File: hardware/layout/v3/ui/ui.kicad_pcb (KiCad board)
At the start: 4 copper layers, 13.8 x 40.5 mm, 25 parts, among them J1 Carrier, J2 OLED ZIF, SW1 PRG/RST, SW2 FUNC, U1 74AHCT1G125

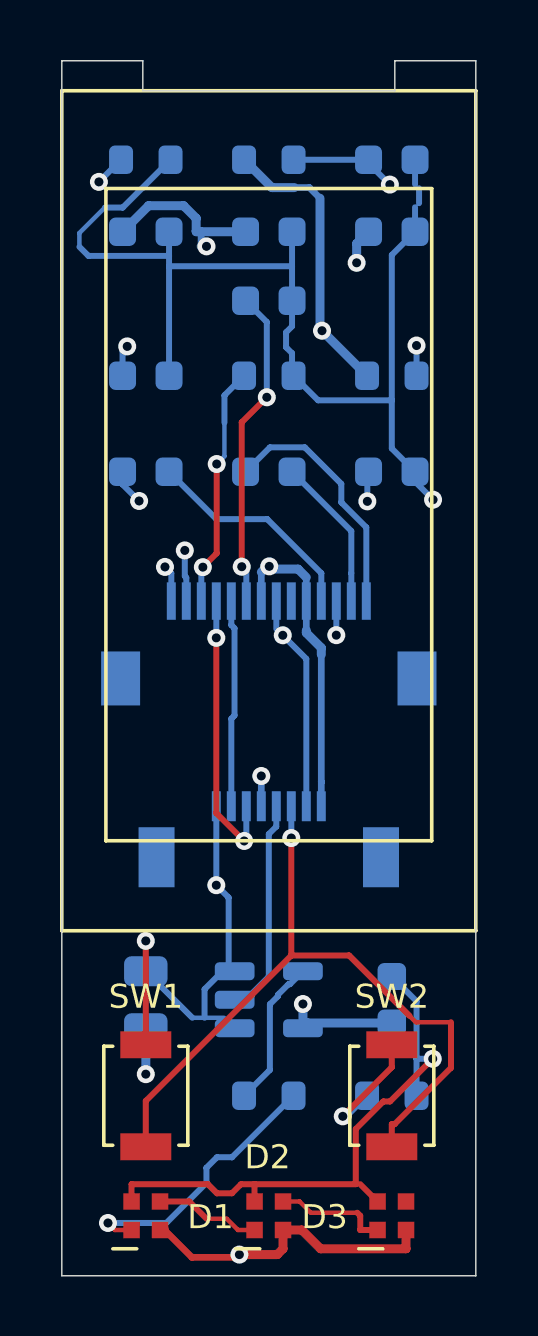
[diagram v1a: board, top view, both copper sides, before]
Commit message: Replaced V3 OLED connector from 14-pin 0.5mm ZIF FPC to 14-pin 0.62mm pitch direct-solder FPC footprint, relocated UI board passives to accommodate new layout with top-edge notch adjusted to 9.8mm width for 12mm flex tail, and updated assembly documentation with NFP1312-15AY part number and pre-applied mounting tape details
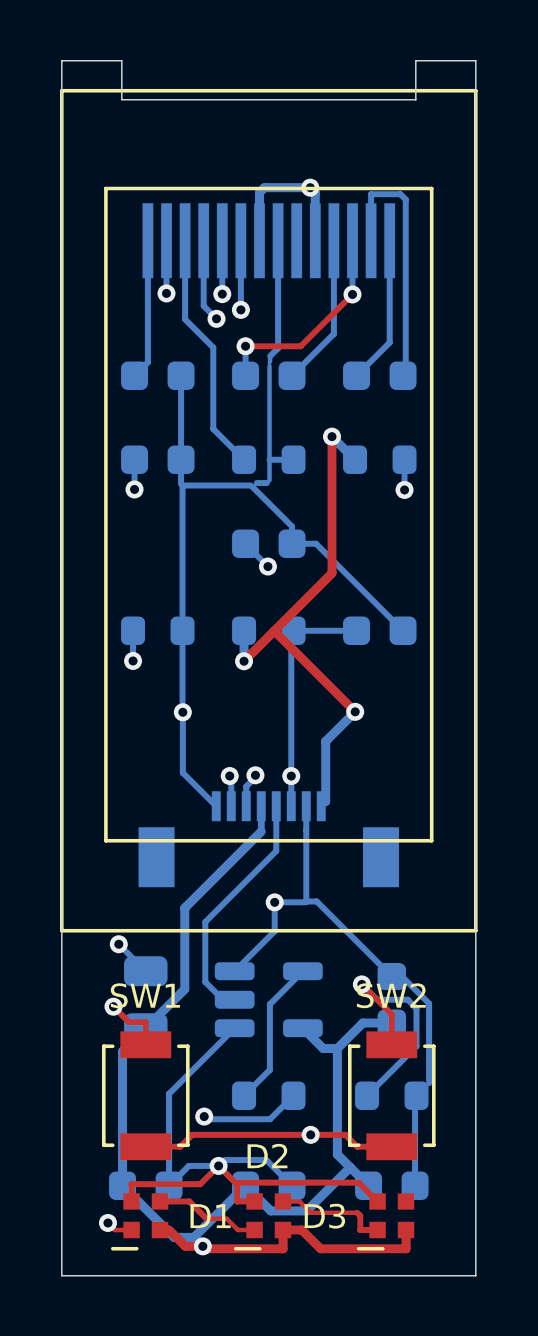
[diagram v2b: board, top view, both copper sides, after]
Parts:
- J2: value OLED ZIF -> OLED; footprint gateway_fp:FPC_XUNPU_FPC-05F-14PH20 -> gateway_fp:OLED_FPC_14P_P0.62mm_Hotbar
- moved C4 31.8 mm to (2.80, -3.00)
- moved C5 31.8 mm to (6.90, -3.00)
- moved C6 31.8 mm to (11.0, -3.00)
- moved C1 15.7 mm to (10.6, -21.5)
- moved R2 15.7 mm to (3.20, -21.5)
- moved R1 15.7 mm to (6.90, -21.5)
- moved J2 13.3 mm to (6.90, -34.5)
- moved C7 8.10 mm to (6.90, -24.4)
- moved C10 7.81 mm to (3.20, -27.2)
- moved C8 5.20 mm to (6.90, -30.0)
- moved C9 4.89 mm to (10.6, -30.0)
- moved R5 2.83 mm to (10.6, -27.2)
- moved R6 2.80 mm to (6.90, -27.2)
- moved C11 0.40 mm to (3.20, -30.0)
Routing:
- net +5V: track 72.7 -> 43.5 mm, vias 6 -> 1
- net BTN_LADDER: track 53.3 -> 28.7 mm
- net I2C_SCL: track 6.93 -> 24.1 mm, vias 0 -> 2
- net N$1: track 31.0 -> 15.2 mm
- net I2C_SDA: track 9.57 -> 19.9 mm
- net OLED_C1P: track 12.6 -> 7.05 mm
- net OLED_VOUT: track 10.1 -> 4.68 mm, vias 2 -> 0
- net N$2: track 4.16 -> 8.17 mm
- net OLED_C2N: track 5.13 -> 8.69 mm
- net OLED_C2P: track 8.28 -> 4.96 mm
- net +3V3: track 29.7 -> 32.1 mm, vias 2 -> 4
- net OLED_C1N: track 7.40 -> 5.08 mm
- net OLED_VCOMH: track 11.0 -> 9.72 mm
- net LED_DATA: track 7.24 -> 8.06 mm
- net N$4: track 9.12 -> 9.10 mm, vias 1 -> 2
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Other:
- outline, holes or cut-outs redrawn
